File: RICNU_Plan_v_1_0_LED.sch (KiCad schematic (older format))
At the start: 8 parts

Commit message: Design freeze - ordered the board
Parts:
- D6: value LED -> LED_R
- D7: value LED -> LED_Y
- D8: value LED -> LED_G
- D9: value LED -> LED_B
- R78: value R -> 660
- R79: value R -> 470
- R80: value R -> 330
- R81: value R -> 180
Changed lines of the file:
@@
 P 5850 3050
 F 0 "D6" H 5650 3100 50  0000 C CNN
-F 1 "LED" H 6000 3000 50  0000 C CNN
+F 1 "LED_R" H 6000 3000 50  0000 C CNN
 F 2 "LEDs:LED_0402" H 5850 3050 50  0001 C CNN
 F 3 "" H 5850 3050 50  0001 C CNN
@@
 P 5850 3250
 F 0 "D7" H 5650 3300 50  0000 C CNN
-F 1 "LED" H 6000 3200 50  0000 C CNN
+F 1 "LED_Y" H 6000 3200 50  0000 C CNN
 F 2 "LEDs:LED_0402" H 5850 3250 50  0001 C CNN
 F 3 "" H 5850 3250 50  0001 C CNN
@@
 P 5850 3450
 F 0 "D8" H 5650 3500 50  0000 C CNN
-F 1 "LED" H 6000 3400 50  0000 C CNN
+F 1 "LED_G" H 6000 3400 50  0000 C CNN
 F 2 "LEDs:LED_0402" H 5850 3450 50  0001 C CNN
 F 3 "" H 5850 3450 50  0001 C CNN
@@
 P 5850 3650
 F 0 "D9" H 5650 3700 50  0000 C CNN
-F 1 "LED" H 6000 3600 50  0000 C CNN
+F 1 "LED_B" H 6000 3600 50  0000 C CNN
 F 2 "LEDs:LED_0402" H 5850 3650 50  0001 C CNN
 F 3 "" H 5850 3650 50  0001 C CNN
@@
 P 4850 3050
 F 0 "R78" V 4900 3250 50  0000 C CNN
-F 1 "R" V 4850 3050 50  0000 C CNN
+F 1 "660" V 4850 3050 50  0000 C CNN
 F 2 "Resistors_SMD:R_0402_NoSilk" V 4780 3050 50  0001 C CNN
 F 3 "" H 4850 3050 50  0001 C CNN
@@
 P 4850 3250
 F 0 "R79" V 4900 3450 50  0000 C CNN
-F 1 "R" V 4850 3250 50  0000 C CNN
+F 1 "470" V 4850 3250 50  0000 C CNN
 F 2 "Resistors_SMD:R_0402_NoSilk" V 4780 3250 50  0001 C CNN
 F 3 "" H 4850 3250 50  0001 C CNN
@@
 P 4850 3450
 F 0 "R80" V 4900 3650 50  0000 C CNN
-F 1 "R" V 4850 3450 50  0000 C CNN
+F 1 "330" V 4850 3450 50  0000 C CNN
 F 2 "Resistors_SMD:R_0402_NoSilk" V 4780 3450 50  0001 C CNN
 F 3 "" H 4850 3450 50  0001 C CNN
@@
 P 4850 3650
 F 0 "R81" V 4900 3850 50  0000 C CNN
-F 1 "R" V 4850 3650 50  0000 C CNN
+F 1 "180" V 4850 3650 50  0000 C CNN
 F 2 "Resistors_SMD:R_0402_NoSilk" V 4780 3650 50  0001 C CNN
 F 3 "" H 4850 3650 50  0001 C CNN
@@
 $EndComp
 $Comp
-L +3V3 #PWR079
+L +3V3 #PWR083
 U 1 1 59FCC29E
 P 4500 2900
-F 0 "#PWR079" H 4500 2750 50  0001 C CNN
+F 0 "#PWR083" H 4500 2750 50  0001 C CNN
 F 1 "+3V3" H 4500 3040 50  0000 C CNN
 F 2 "" H 4500 2900 50  0001 C CNN

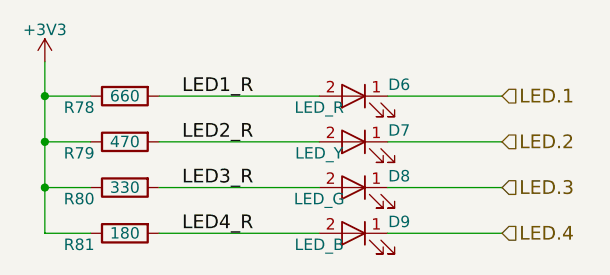
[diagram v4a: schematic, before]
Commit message: Various small changes like comment removal
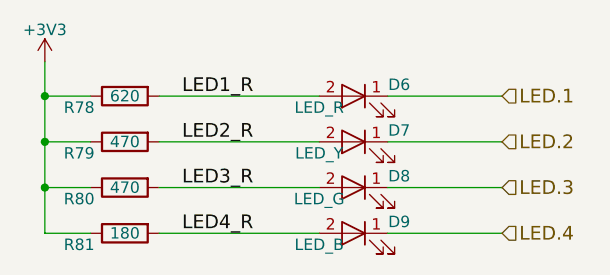
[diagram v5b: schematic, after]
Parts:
- R78: value 660 -> 620
- R80: value 330 -> 470
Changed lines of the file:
@@
 P 4850 3050
 F 0 "R78" V 4900 3250 50  0000 C CNN
-F 1 "660" V 4850 3050 50  0000 C CNN
+F 1 "620" V 4850 3050 50  0000 C CNN
 F 2 "Resistors_SMD:R_0402_NoSilk" V 4780 3050 50  0001 C CNN
 F 3 "" H 4850 3050 50  0001 C CNN
@@
 P 4850 3450
 F 0 "R80" V 4900 3650 50  0000 C CNN
-F 1 "330" V 4850 3450 50  0000 C CNN
+F 1 "470" V 4850 3450 50  0000 C CNN
 F 2 "Resistors_SMD:R_0402_NoSilk" V 4780 3450 50  0001 C CNN
 F 3 "" H 4850 3450 50  0001 C CNN
